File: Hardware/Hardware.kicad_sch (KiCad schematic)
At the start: 1 part, among them U1 Teensy4.1_DEV-16771

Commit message: Added things (very nice)
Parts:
- removed U1: Teensy4.1_DEV-16771, MODULE_DEV-16771, symbol MRDT_Shields:Teensy4.1_DEV-16771
- added C1: 0.1 uF, symbol Device:C
- added J2: RJ45_LED_Shielded, symbol Connector:RJ45_LED_Shielded
- added U2: CR2013-MI2120, Display:CR2013-MI2120, symbol Driver_Display:CR2013-MI2120
- added U3: Teensy4.1_DEV-16771, MODULE_DEV-16771, symbol MRDT_Shields:Teensy4.1_DEV-16771
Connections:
- new net: C1.1, J2.2, J2.5
- new net: U3.GND1 (GND), U3.GND2 (GND), U3.GND3 (GND), U3.GND4 (GND), U3.GND5 (GND)
- new net: U3.USB_GND1 (USB_GND), U3.USB_GND2 (USB_GND)
- new net +3.3V: U3.3.3V_1 (3.3V), U3.3.3V_2 (3.3V), U3.3.3V_3 (3.3V)
- new net GND: C1.2, J2.8, J2.9, J2.SH
- new net LED: J2.10, U3.LED
- new net Rx+: J2.4, U3.R+
- new net Rx-: J2.6, U3.R-
- new net Tx+: J2.1, U3.T+
- new net Tx-: J2.3, U3.T-
- no-connect marks 0 -> 17

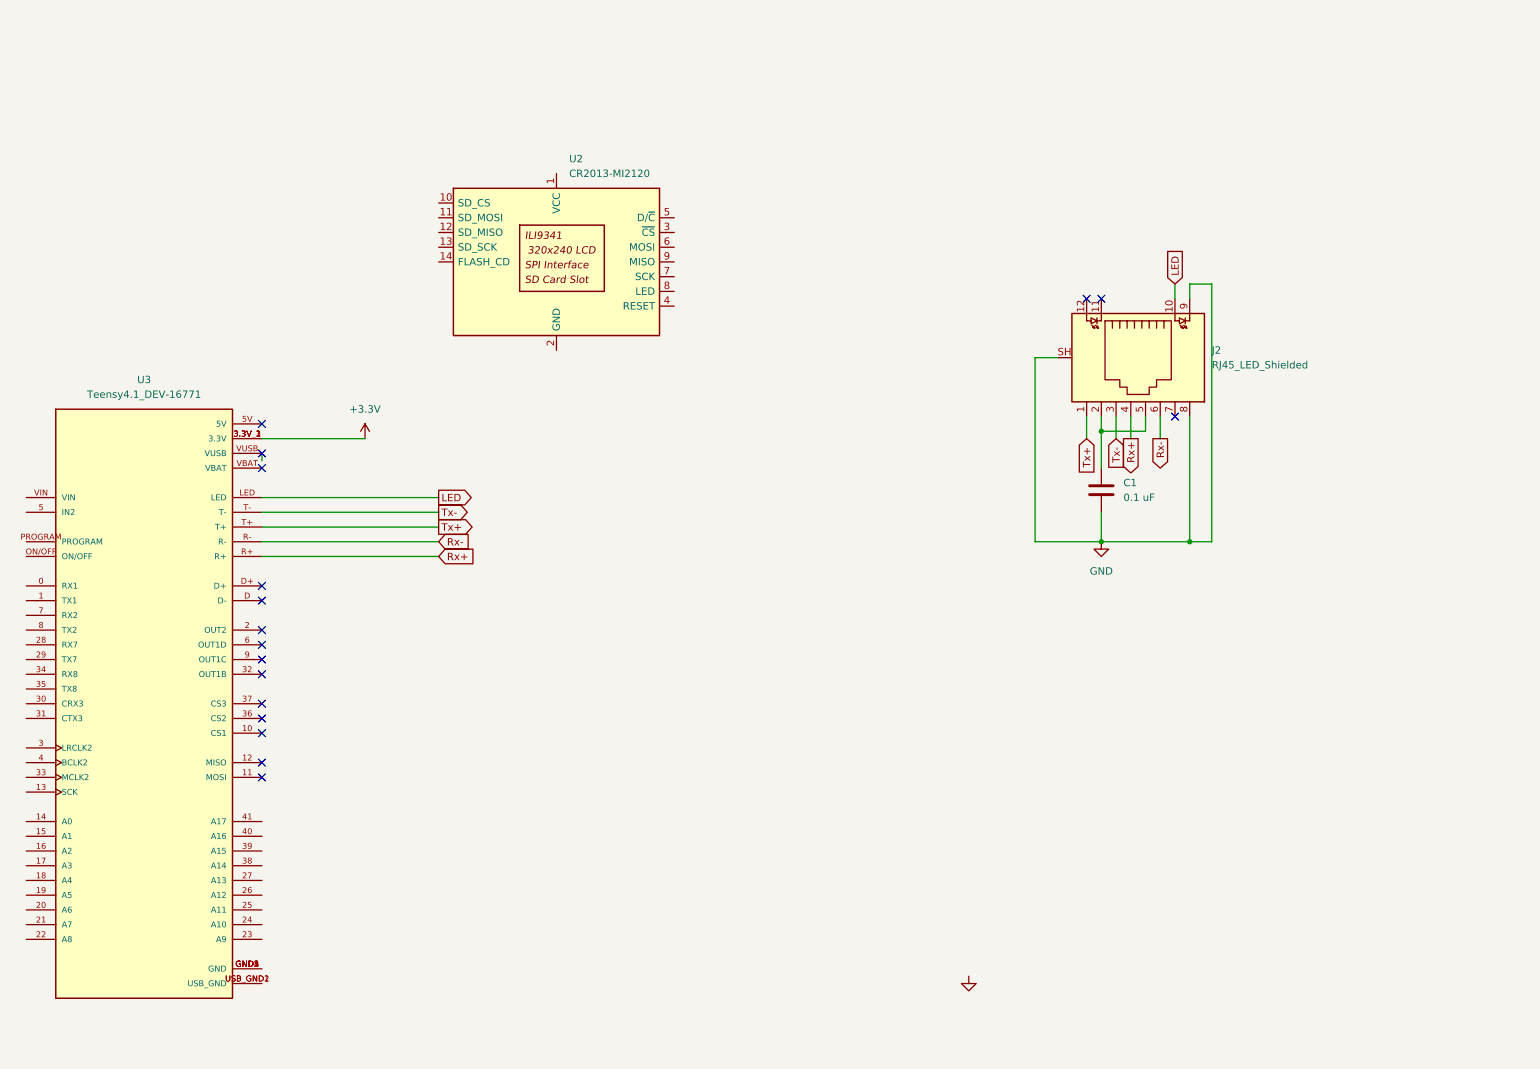
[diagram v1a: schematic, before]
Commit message: connected teensy pins to LCD socket
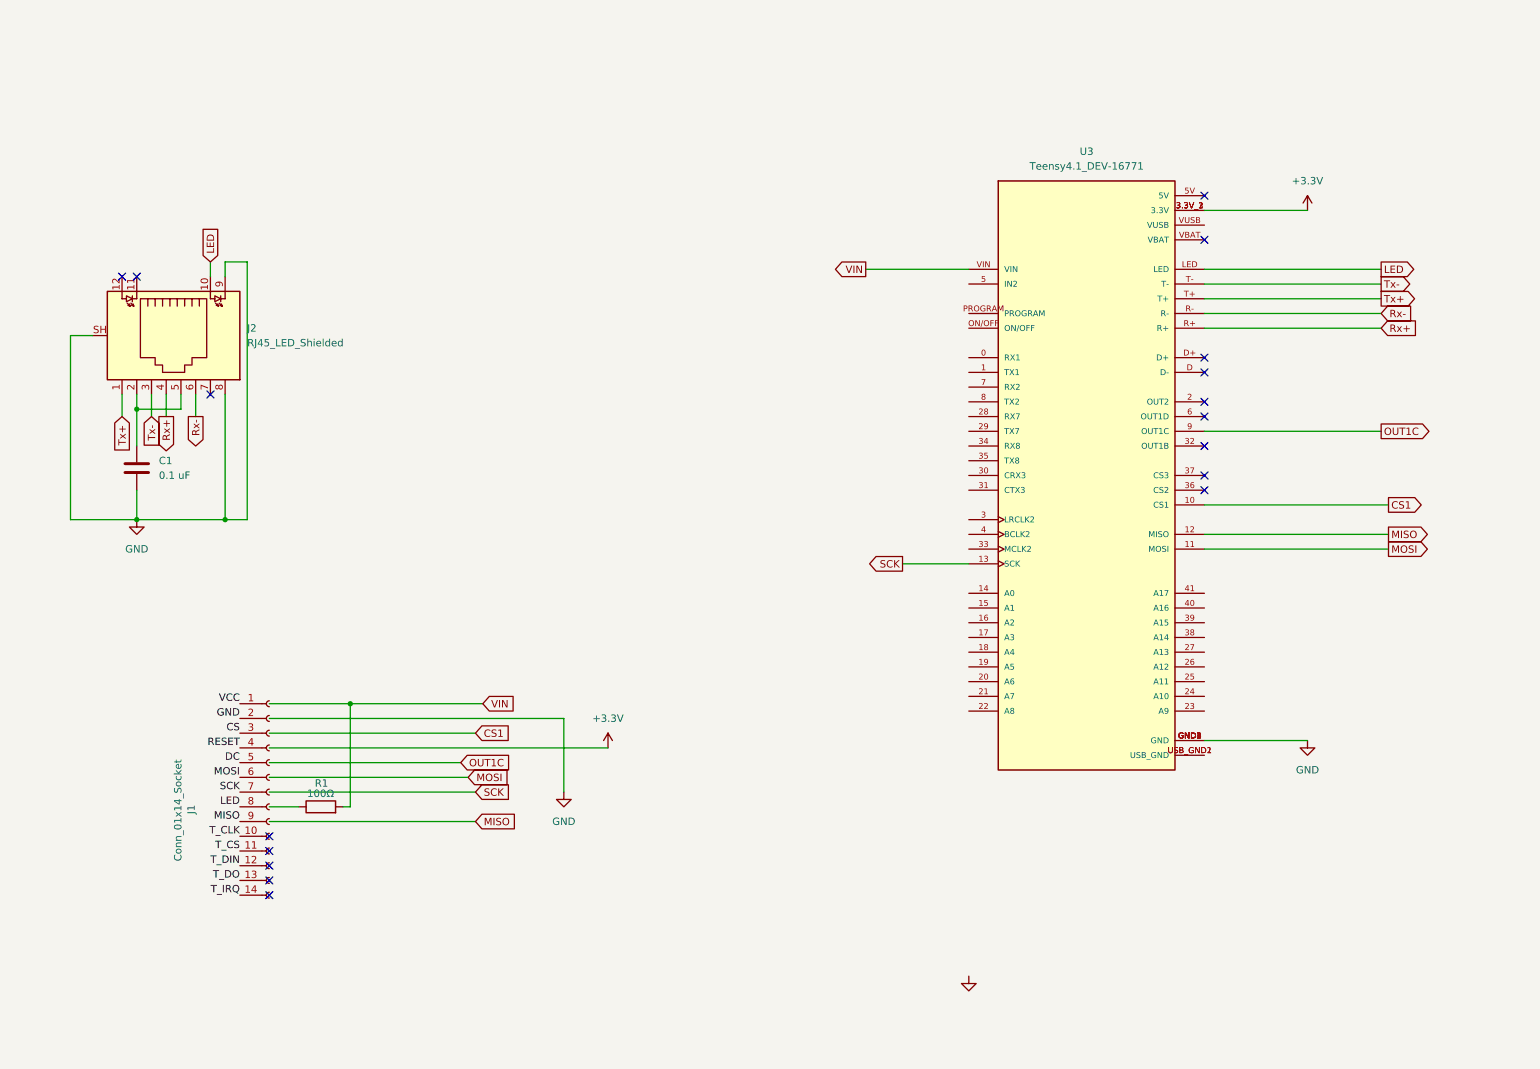
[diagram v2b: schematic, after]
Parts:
- removed U2: CR2013-MI2120, Display:CR2013-MI2120, symbol Driver_Display:CR2013-MI2120
- added J1: Conn_01x14_Socket, symbol Connector:Conn_01x14_Socket
- added R1: 100Ω, symbol Device:R
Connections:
- net GND: now also U3.GND1 (GND), U3.GND2 (GND), U3.GND3 (GND), U3.GND4 (GND), U3.GND5 (GND), J1.2 (Pin_2)
- net LED: now also J1.8 (Pin_8)
- net CS1: now reaches U3.10 (CS1)
- net MOSI: now reaches U3.11 (MOSI)
- net MOSI: now also J1.6 (Pin_6)
- net MISO: now reaches U3.12 (MISO)
- net MISO: now also J1.9 (Pin_9)
- net SCK: now reaches U3.13 (SCK)
- net SCK: now also J1.7 (Pin_7)
- net OUT1C: now reaches U3.9 (OUT1C)
- net VIN: now reaches U3.VIN
- net VIN: now also R1.2
- new net CS: J1.3 (Pin_3)
- new net DC: J1.5 (Pin_5)
- new net RESET: J1.4 (Pin_4)
- new net T_CLK: J1.10 (Pin_10)
- new net T_CS: J1.11 (Pin_11)
- new net T_DIN: J1.12 (Pin_12)
- new net T_DO: J1.13 (Pin_13)
- new net T_IRQ: J1.14 (Pin_14)
- new net VCC: J1.1 (Pin_1)
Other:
- moved on the sheet: C1, J2, U3

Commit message: Fixed schematic errors, mapped touchscreen pins for the lcd
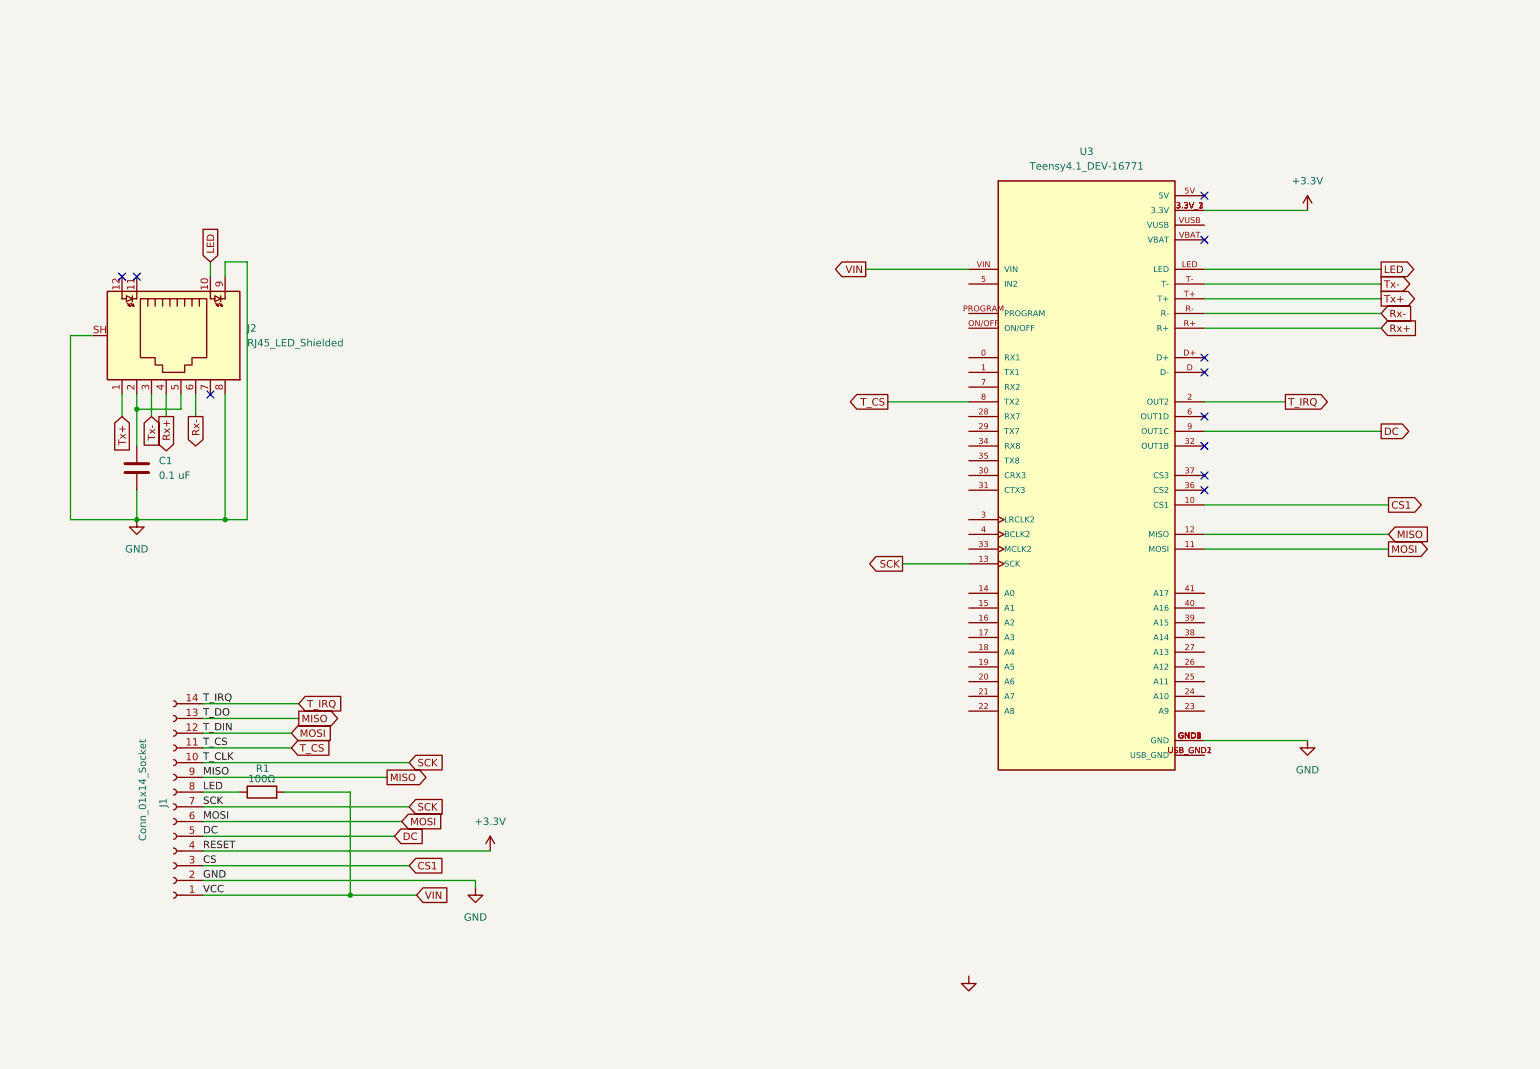
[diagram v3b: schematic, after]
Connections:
- net CS is gone; now on net CS1: J1.3 (Pin_3)
- net OUT1C is gone; now on net DC: U3.9 (OUT1C)
- net RESET is gone; now on net +3.3V: J1.4 (Pin_4)
- net T_CLK is gone; now on net SCK: J1.10 (Pin_10)
- net T_DIN is gone; now on net MOSI: J1.12 (Pin_12)
- net T_DO is gone; now on net MISO: J1.13 (Pin_13)
- net VCC is gone; now on net VIN: J1.1 (Pin_1)
- net LED: now also R1.1
- net T_CS: now also U3.8 (TX2)
- net T_IRQ: now also U3.2 (OUT2)
- no-connect marks 17 -> 11
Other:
- moved on the sheet: J1, R1

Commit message: Added battery/voltage regulator
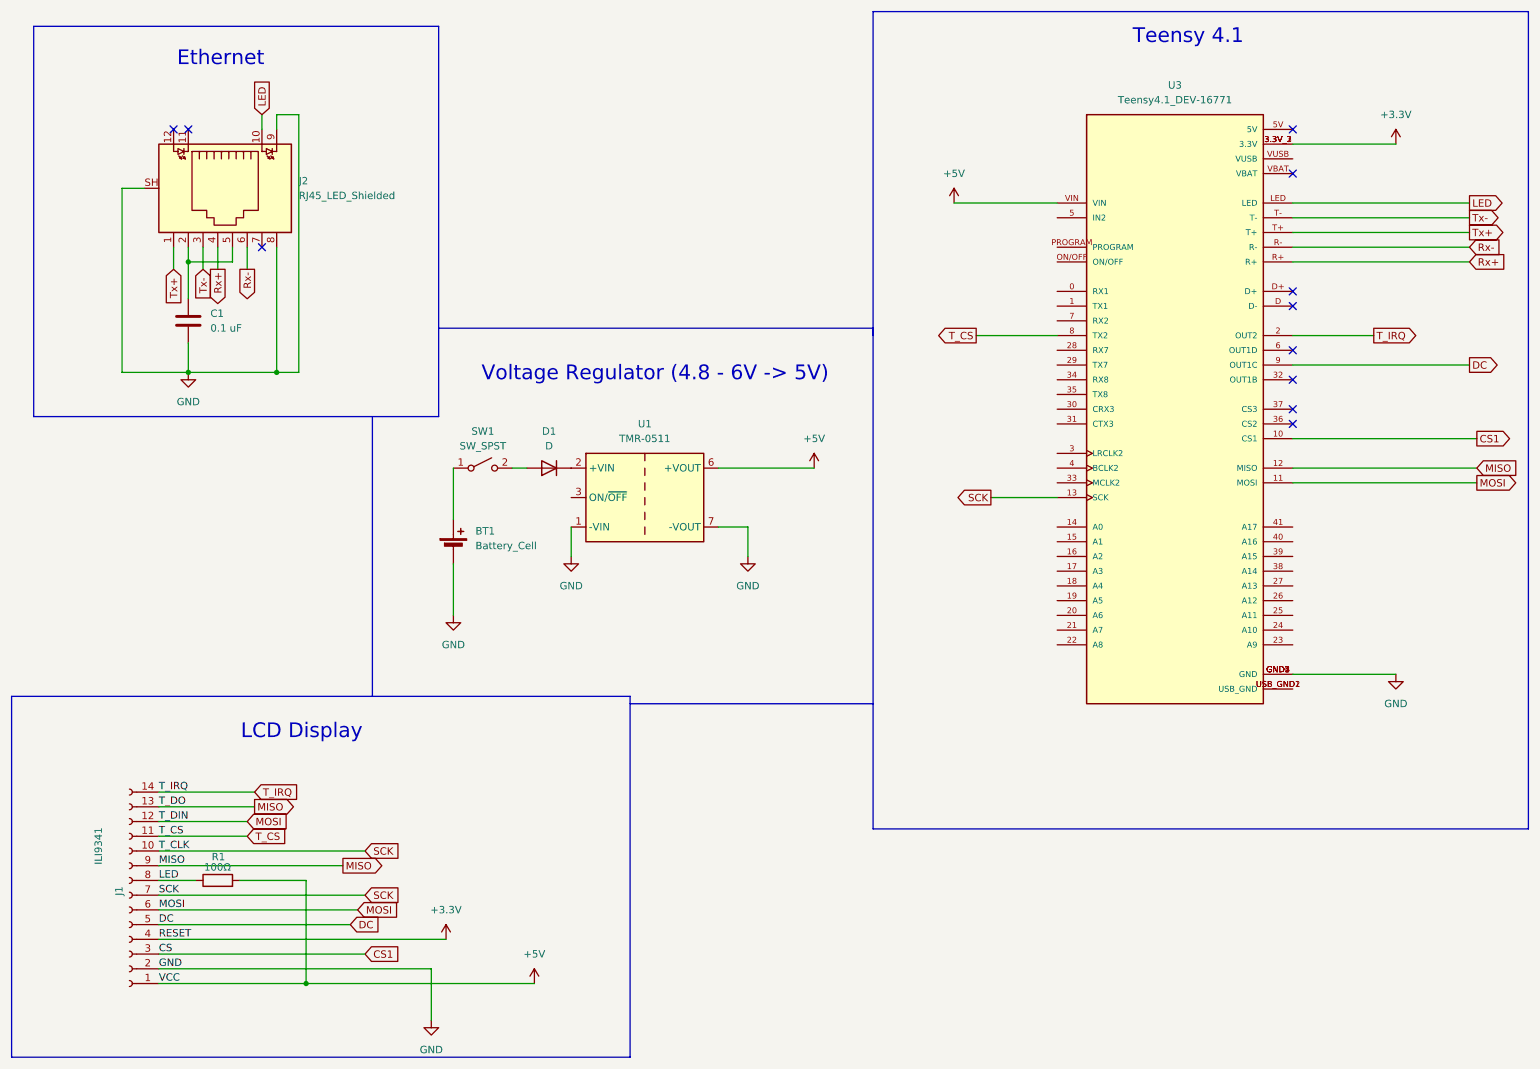
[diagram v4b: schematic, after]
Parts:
- added BT1: Battery_Cell, symbol Device:Battery_Cell
- added D1: D, symbol Device:D
- added SW1: SW_SPST, symbol Switch:SW_SPST
- added U1: TMR-0511, Converter_DCDC:Converter_DCDC_TRACO_TMR-xxxx_THT, symbol Converter_DCDC:TMR-0511
- J1: value Conn_01x14_Socket -> ILI9341
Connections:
- net GND: now also BT1.2 (-), U1.1 (-VIN), U1.7 (-VOUT)
- net VIN renamed +5V
- net +5V: now also U1.6 (+VOUT)
- new net: BT1.1 (+), SW1.1 (A)
- new net: D1.2 (A), SW1.2 (B)
- new net: D1.1 (K), U1.2 (+VIN)
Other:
- note added: "Ethernet"
- note added: "LCD Display"
- note added: "Teensy 4.1"
- note added: "Voltage Regulator (4.8 - 6V -> 5V)"
- moved on the sheet: C1, J1, J2, R1, U3

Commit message: moved things around to make space for CAN tranceiver and keypad
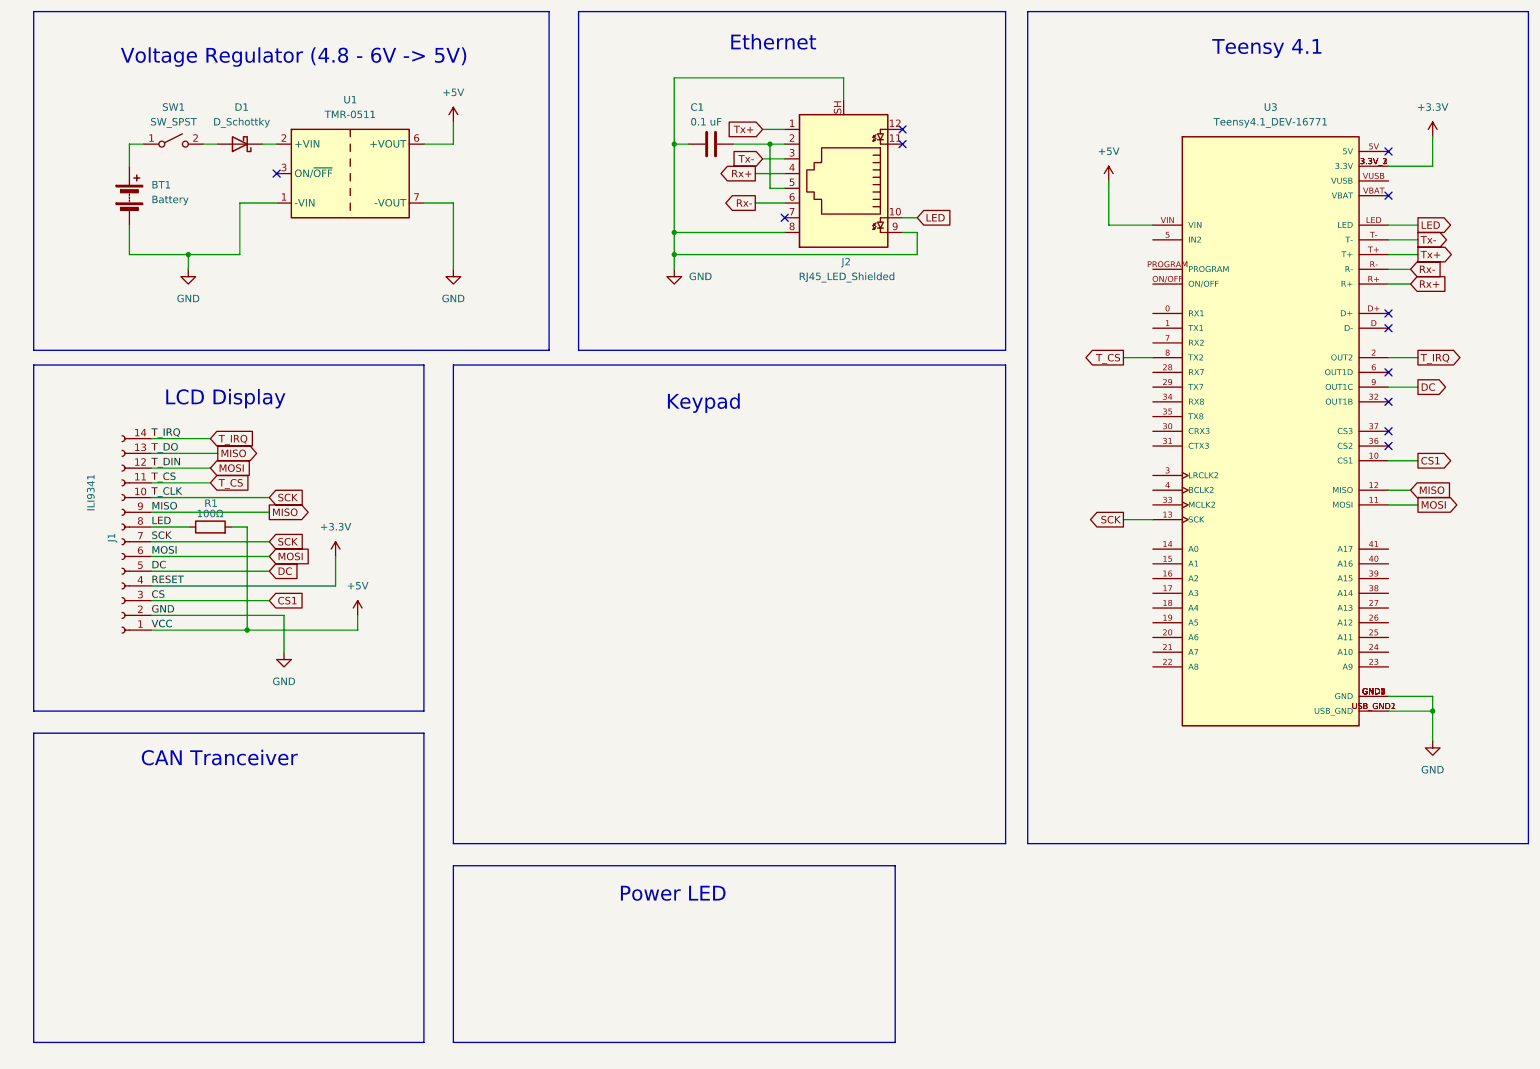
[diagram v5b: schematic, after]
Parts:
- removed BT1: Battery_Cell, symbol Device:Battery_Cell
- removed D1: D, symbol Device:D
- added BT1: Battery, symbol Device:Battery
- added D1: D_Schottky, symbol Device:D_Schottky
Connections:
- net GND: now also U3.USB_GND1 (USB_GND), U3.USB_GND2 (USB_GND), BT1.2 (-)
- net at SW1.1 (A): now also BT1.1 (+)
- net at SW1.2 (B): now also D1.2 (A)
- net at U1.2 (+VIN): now also D1.1 (K)
- no-connect marks 11 -> 12
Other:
- note added: "CAN Tranceiver"
- note added: "Keypad"
- note added: "Power LED"
- moved on the sheet: C1, J1, J2, R1, SW1, U1, U3
